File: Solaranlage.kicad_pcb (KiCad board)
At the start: 2 copper layers, 160 x 85 mm, 77 parts, among them J1 Screw_Terminal_01x02, J2 Screw_Terminal_01x02, J3 AVR-JTAG-10, J4 USB_B, J5 USB_B, J6 Screw_Terminal_01x02, Q1 2N3904, SW1 Rotary_Encoder_Switch_Panason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, SW2 SW_SPDT, U1 SC56-11E*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

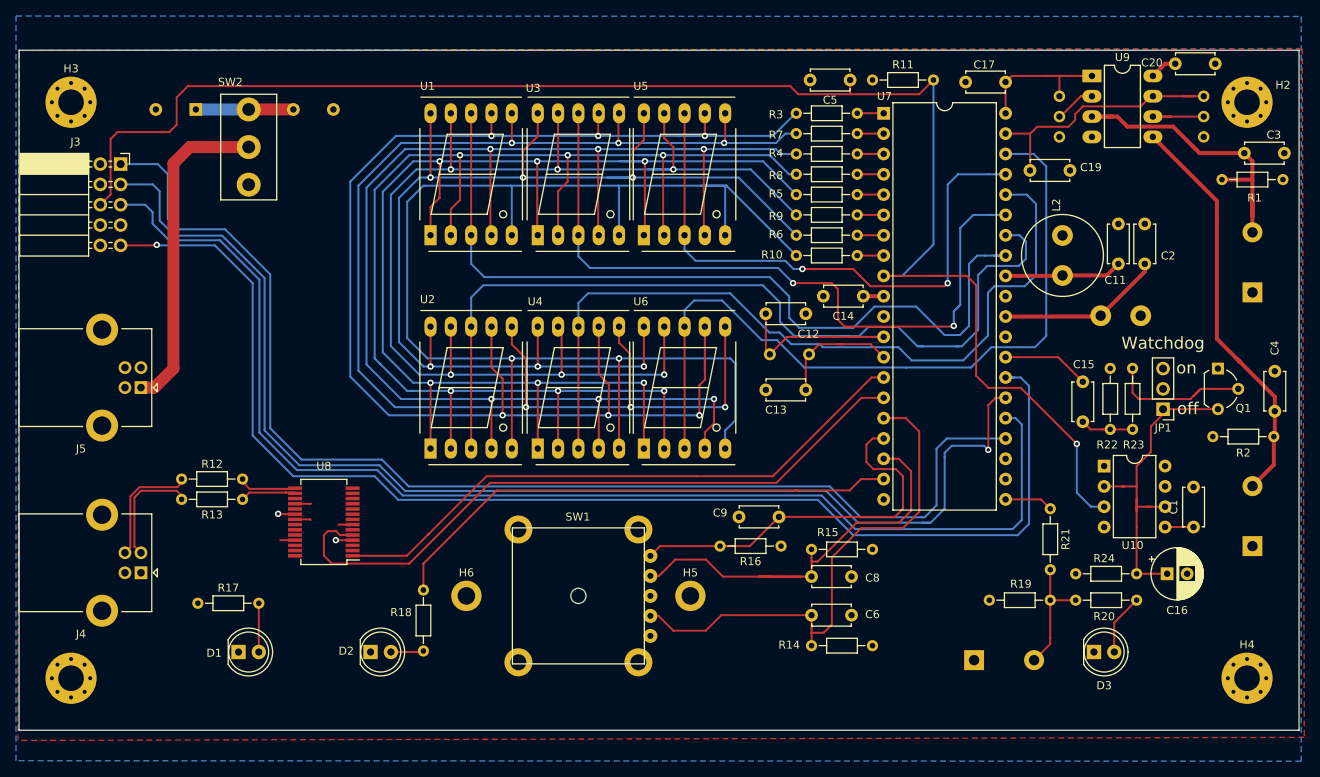
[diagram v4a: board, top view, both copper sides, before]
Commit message: added LEDs to indicate what the displays show at the moment; added some 3D models; added 10k serial resistors to opamp-outs for TP
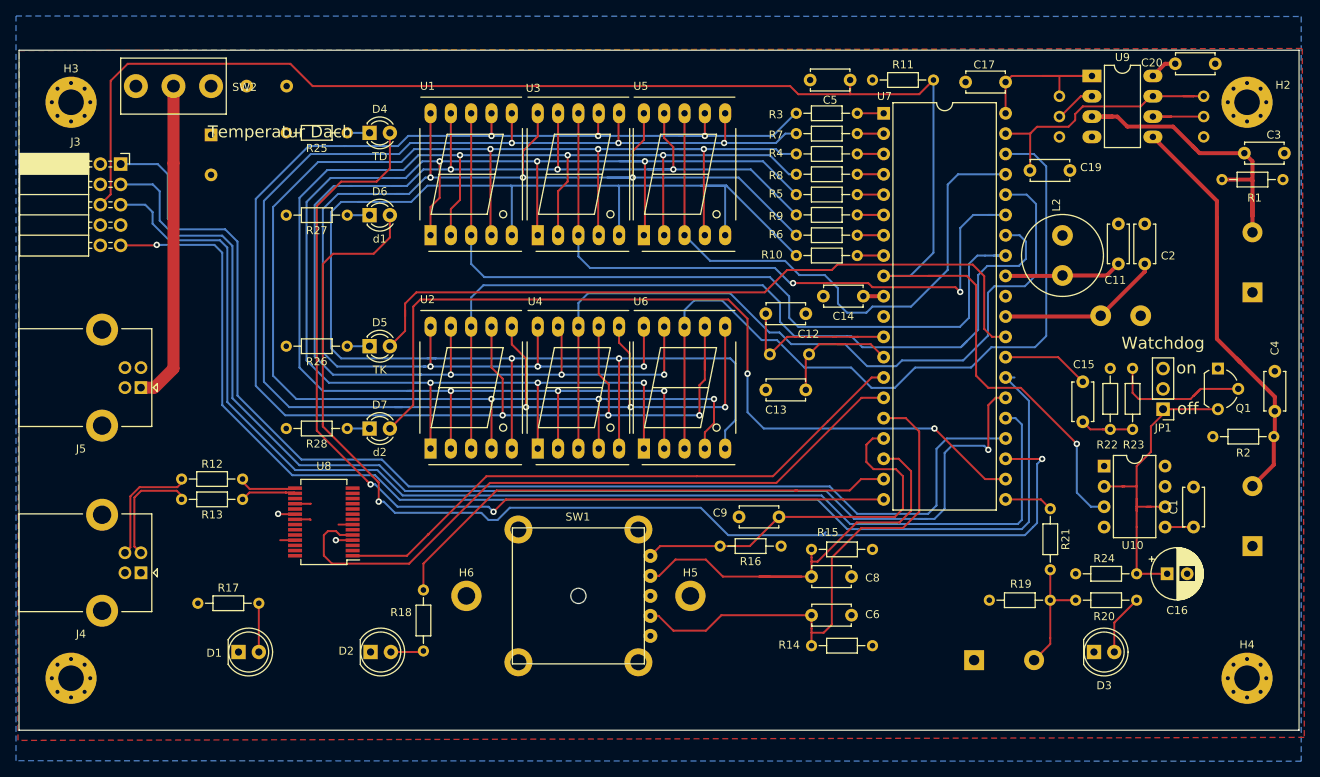
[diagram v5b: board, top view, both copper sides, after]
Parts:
- added D4: TD, LED_THT:LED_D3.0mm, F.Cu at (112.9, 65.5)
- added D5: TK, LED_THT:LED_D3.0mm, F.Cu at (112.9, 92.2)
- added D6: d1, LED_THT:LED_D3.0mm, F.Cu at (112.9, 75.8)
- added D7: d2, LED_THT:LED_D3.0mm, F.Cu at (112.9, 102.5)
- added R25: 330, Resistor_THT:R_Axial_DIN0204_L3.6mm_D1.6mm_P7.62mm_Horizontal, F.Cu at (110.1, 65.5)
- added R26: 330, Resistor_THT:R_Axial_DIN0204_L3.6mm_D1.6mm_P7.62mm_Horizontal, F.Cu at (110.1, 92.2)
- added R27: 330, Resistor_THT:R_Axial_DIN0204_L3.6mm_D1.6mm_P7.62mm_Horizontal, F.Cu at (110.1, 75.8)
- added R28: 330, Resistor_THT:R_Axial_DIN0204_L3.6mm_D1.6mm_P7.62mm_Horizontal, F.Cu at (110.1, 102.5)
- moved SW2 12.1 mm to (88.4, 59.7), turned to 180 degrees
- moved C7 6.53 mm to (97.5, 59.7)
- moved C18 3.70 mm to (93.1, 65.8), turned to 270 degrees
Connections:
- H1 pad 1: (no net) -> GND
- H2 pad 1: (no net) -> GND
- H3 pad 1: (no net) -> GND
- H4 pad 1: (no net) -> GND
- H5 pad 1: (no net) -> GND
- H6 pad 1: (no net) -> GND
- U7 pad 20: Net-(U7-Pad20) -> delta2
- U7 pad 22: Net-(U7-Pad22) -> temp_dach
- U7 pad 23: Net-(U7-Pad23) -> temp_keller
- U7 pad 29: Net-(U7-Pad29) -> delta1
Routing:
- net temp_keller: track 0.00 -> 145.1 mm, vias 0 -> 2
- net delta2: track 0.00 -> 119.3 mm, vias 0 -> 2
- net temp_dach: track 0.00 -> 107.0 mm, vias 0 -> 2
- net delta1: track 0.00 -> 93.0 mm
- net /C_2: track 178.0 -> 203.3 mm
- net /B_2: track 174.4 -> 198.7 mm
- net /A_2: track 176.9 -> 200.2 mm
- net /DP_2: track 168.2 -> 189.1 mm
- net /F_2: track 151.7 -> 172.3 mm
- net /G_2: track 147.6 -> 167.9 mm
- net /E_2: track 165.8 -> 185.8 mm
- net /D_2: track 179.9 -> 199.5 mm
- net +5V: track 22.6 -> 10.2 mm
- net /DZ: track 90.9 -> 82.3 mm
- net \RST: track 199.0 -> 204.2 mm
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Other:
- board text added: "Temperatur Dach"

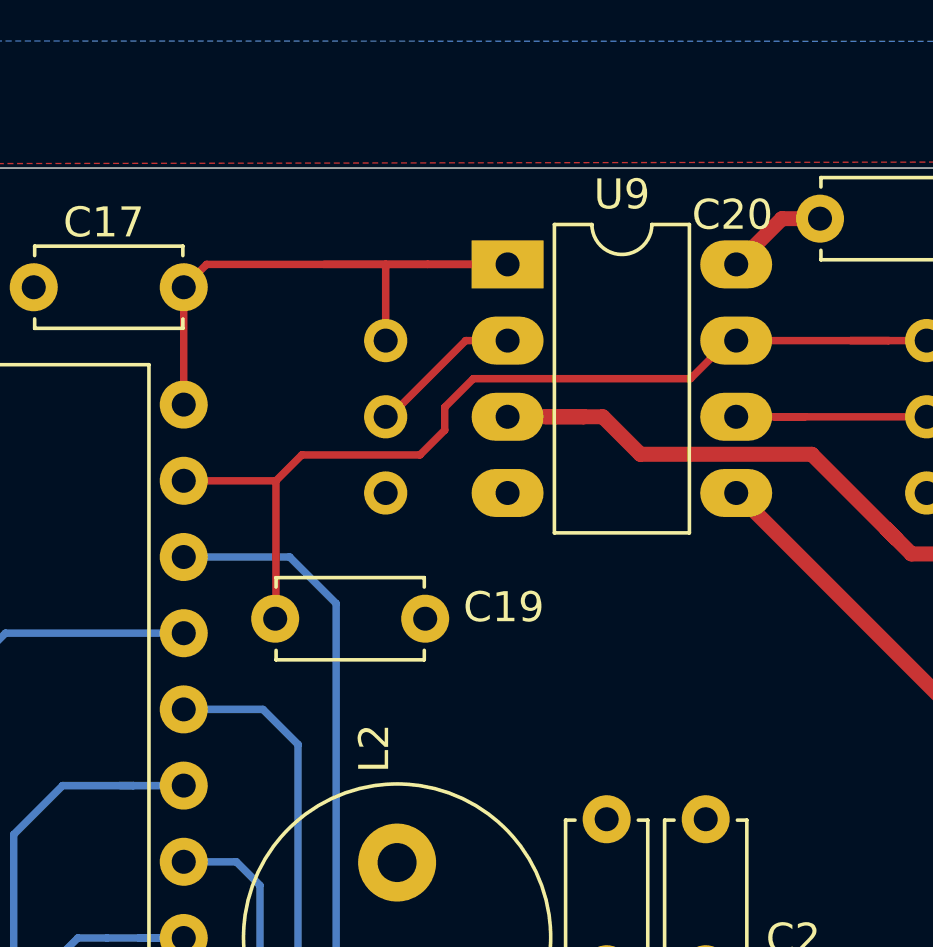
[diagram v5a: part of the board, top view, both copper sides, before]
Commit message: added resistors to layout
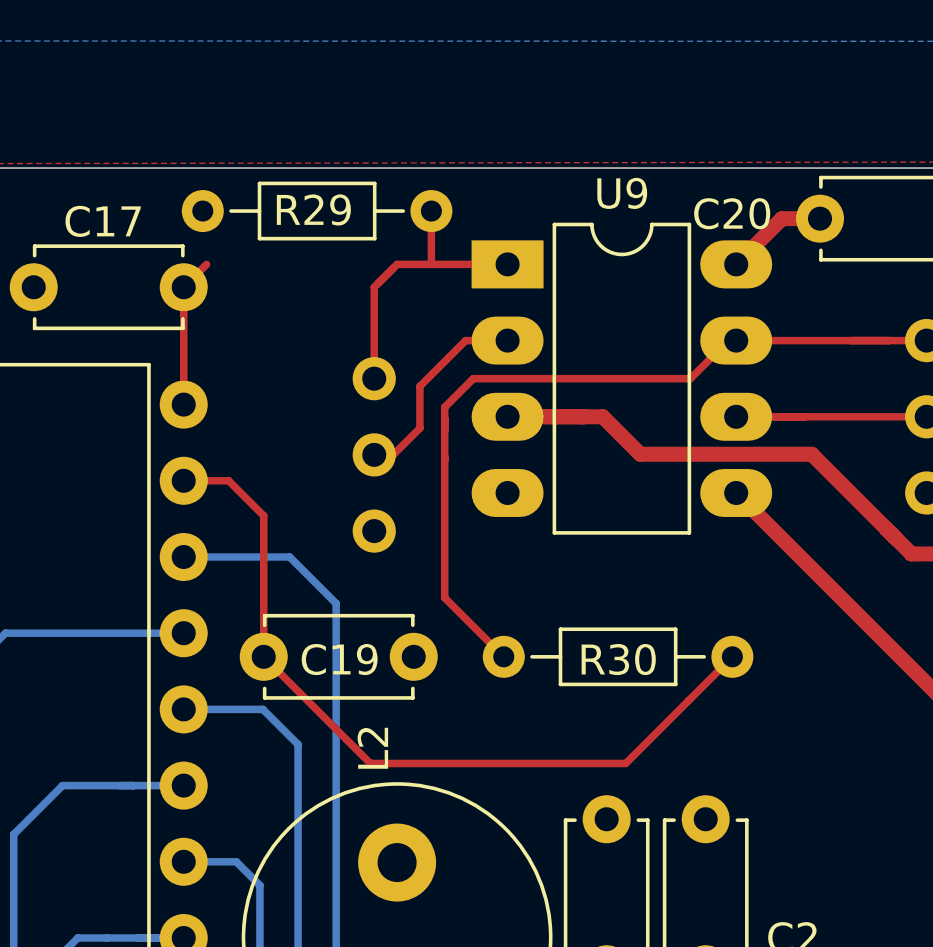
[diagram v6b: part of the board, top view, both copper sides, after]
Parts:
- added R29: 10k, Resistor_THT:R_Axial_DIN0204_L3.6mm_D1.6mm_P7.62mm_Horizontal, F.Cu at (193.0, 56.6)
- added R30: 10k, Resistor_THT:R_Axial_DIN0204_L3.6mm_D1.6mm_P7.62mm_Horizontal, F.Cu at (210.7, 71.5)
- C17, C19: value 10n -> 100n
- moved C19 1.33 mm to (195.1, 71.5)
- moved RV1 1.33 mm to (198.8, 62.2)
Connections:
- RV1 pad 1: /DACH_ADC -> Net-(R29-Pad2)
- RV2 pad 1: /KELLER_ADC -> Net-(R30-Pad2)
- U9 pad 1: /DACH_ADC -> Net-(R29-Pad2)
- U9 pad 7: /KELLER_ADC -> Net-(R30-Pad2)
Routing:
- net Net-(R30-Pad2): track 0.00 -> 27.9 mm
- net /DACH_ADC: track 23.7 -> 4.99 mm
- net Net-(R29-Pad2): track 0.00 -> 10.3 mm
- net /KELLER_ADC: track 33.1 -> 26.4 mm
- net Net-(RV1-Pad2): track 5.12 -> 6.84 mm

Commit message: optimization layout
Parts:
- moved RV2 1.27 mm to (217.2, 62.2)
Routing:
- net Net-(R30-Pad2): track 27.9 -> 33.5 mm
- net Net-(C3-Pad1): track 39.4 -> 38.5 mm
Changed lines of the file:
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@@
     (thickness 1.6)
     (drawings 14)
-    (tracks 866)
+    (tracks 868)
     (zones 0)
     (modules 87)
@@
   (setup
     (last_trace_width 0.25)
+    (user_trace_width 0)
     (user_trace_width 0.2)
     (user_trace_width 0.5)
+    (user_trace_width 0.5)
     (user_trace_width 1.5)
     (trace_clearance 0.2)
@@
   )
   (module Potentiometer_THT:Potentiometer_Bourns_3299W_Vertical (layer B.Cu)
-    (at 217.17 60.96 90)
+    (at 217.17 62.23 90)
     (descr "Potentiometer, vertical, Bourns 3299W, https://www.bourns.com/pdfs/3299.pdf")
     (tags "Potentiometer vertical Bourns 3299W")
@@
     (descr "Inductor, Radial series, Radial, pin pitch=5.00mm, , diameter=10mm, Fastron, 07P, http://www.fastrongroup.com/image-show/37/07M.pdf?type=Complete-DataSheet&productType=series")
     (tags "Inductor Radial series Radial pin pitch 5.00mm  diameter 10mm Fastron 07P")
-    (fp_text reference L2 (at -3.81 0.762 90) (layer F.SilkS)
+    (fp_text reference L2 (at -2.413 4.064 180) (layer F.SilkS)
       (effects (font (size 1 1) (thickness 0.15)))
     )
@@
   (segment (start 223.266 71.501) (end 223.266 70.612) (width 0.5) (layer F.Cu) (net 40))
   (segment (start 223.266 70.612) (end 223.266 69.088) (width 0.5) (layer F.Cu) (net 40))
-  (segment (start 216.662 68.072) (end 215.8365 67.2465) (width 0.5) (layer F.Cu) (net 40))
-  (segment (start 222.25 68.072) (end 216.662 68.072) (width 0.5) (layer F.Cu) (net 40))
-  (segment (start 216.154 67.564) (end 215.8365 67.2465) (width 0.5) (layer F.Cu) (net 40))
-  (segment (start 213.34001 64.75001) (end 207.62501 64.75001) (width 0.5) (layer F.Cu) (net 40))
-  (segment (start 207.62501 64.75001) (end 206.375 63.5) (width 0.5) (layer F.Cu) (net 40))
-  (segment (start 215.8365 67.2465) (end 213.34001 64.75001) (width 0.5) (layer F.Cu) (net 40))
   (segment (start 203.2 63.5) (end 205.74 63.5) (width 0.5) (layer F.Cu) (net 40))
   (segment (start 205.74 63.5) (end 204.47 63.5) (width 0.5) (layer F.Cu) (net 40))
   (segment (start 206.375 63.5) (end 205.74 63.5) (width 0.5) (layer F.Cu) (net 40))
+  (segment (start 212.57801 64.75001) (end 207.62501 64.75001) (width 0.5) (layer F.Cu) (net 40))
+  (segment (start 214.5665 66.7385) (end 212.57801 64.75001) (width 0.5) (layer F.Cu) (net 40))
+  (segment (start 214.5665 68.3895) (end 214.5665 66.7385) (width 0.5) (layer F.Cu) (net 40))
+  (segment (start 207.62501 64.75001) (end 206.375 63.5) (width 0.5) (layer F.Cu) (net 40))
+  (segment (start 217.551 71.374) (end 214.5665 68.3895) (width 0.5) (layer F.Cu) (net 40))
+  (segment (start 219.456 71.374) (end 217.551 71.374) (width 0.5) (layer F.Cu) (net 40))
   (segment (start 225.933 107.023) (end 223.266 109.69) (width 0.5) (layer F.Cu) (net 41))
   (segment (start 225.933 103.505) (end 225.933 107.023) (width 0.5) (layer F.Cu) (net 41))
@@
   (segment (start 226.06 100.33) (end 226.06 98.525) (width 0.5) (layer F.Cu) (net 41))
   (segment (start 221.565 94.03) (end 221.2475 93.7125) (width 0.5) (layer F.Cu) (net 41))
-  (segment (start 218.821 91.286) (end 221.7555 94.2205) (width 0.5) (layer F.Cu) (net 41))
   (segment (start 221.7555 94.2205) (end 221.565 94.03) (width 0.5) (layer F.Cu) (net 41))
   (segment (start 226.06 98.525) (end 221.7555 94.2205) (width 0.5) (layer F.Cu) (net 41))
-  (segment (start 218.821 74.041) (end 210.82 66.04) (width 0.5) (layer F.Cu) (net 41))
-  (segment (start 218.821 76.2) (end 218.821 74.041) (width 0.5) (layer F.Cu) (net 41))
-  (segment (start 218.821 76.2) (end 218.821 91.286) (width 0.5) (layer F.Cu) (net 41))
+  (segment (start 218.821 91.286) (end 221.7555 94.2205) (width 0.5) (layer F.Cu) (net 41))
+  (segment (start 218.821 75.819) (end 218.821 91.286) (width 0.5) (layer F.Cu) (net 41))
+  (segment (start 212.598 69.596) (end 218.821 75.819) (width 0.5) (layer F.Cu) (net 41))
+  (segment (start 212.598 67.818) (end 212.598 69.596) (width 0.5) (layer F.Cu) (net 41))
+  (segment (start 210.82 66.04) (end 212.598 67.818) (width 0.5) (layer F.Cu) (net 41))
   (segment (start 205.994 126.746) (end 208.788 123.952) (width 0.25) (layer F.Cu) (net 42))
   (segment (start 205.994 130.429) (end 205.994 126.746) (width 0.25) (layer F.Cu) (net 42))
@@
   (segment (start 193.167 58.42) (end 192.405 59.182) (width 0.25) (layer F.Cu) (net 43))
   (segment (start 214.63 60.96) (end 215.9 60.96) (width 0.25) (layer F.Cu) (net 92))
-  (segment (start 215.9 60.96) (end 217.17 60.96) (width 0.25) (layer F.Cu) (net 92))
   (segment (start 195.072 66.802) (end 193.9036 65.6336) (width 0.25) (layer F.Cu) (net 44))
   (segment (start 195.072 71.501) (end 195.072 66.802) (width 0.25) (layer F.Cu) (net 44))
@@
   (segment (start 199.39 64.77) (end 200.279 63.881) (width 0.25) (layer F.Cu) (net 80))
   (segment (start 198.755 64.77) (end 199.39 64.77) (width 0.25) (layer F.Cu) (net 80))
-  (segment (start 213.106 63.5) (end 210.82 63.5) (width 0.25) (layer F.Cu) (net 81))
-  (segment (start 212.09 63.5) (end 213.106 63.5) (width 0.25) (layer F.Cu) (net 81))
-  (segment (start 213.106 63.5) (end 217.17 63.5) (width 0.25) (layer F.Cu) (net 81))
+  (segment (start 217.17 64.77) (end 215.392 64.77) (width 0.25) (layer F.Cu) (net 81))
+  (segment (start 215.392 64.77) (end 214.122 63.5) (width 0.25) (layer F.Cu) (net 81))
+  (segment (start 214.122 63.5) (end 210.82 63.5) (width 0.25) (layer F.Cu) (net 81))
   (segment (start 196.8246 111.3536) (end 197.993 112.522) (width 0.25) (layer F.Cu) (net 82))
   (segment (start 192.405 111.3536) (end 196.8246 111.3536) (width 0.25) (layer F.Cu) (net 82))
@@
   (segment (start 201.1045 64.8335) (end 201.1045 69.5325) (width 0.25) (layer F.Cu) (net 92))
   (segment (start 201.1045 64.8335) (end 201.1045 64.9605) (width 0.25) (layer F.Cu) (net 92))
+  (segment (start 215.9 60.96) (end 217.17 62.23) (width 0.25) (layer F.Cu) (net 92))
+  (segment (start 210.82 60.96) (end 215.9 60.96) (width 0.25) (layer F.Cu) (net 92))
   (zone (net 2) (net_name +5V) (layer B.Cu) (hatch edge 0.508)
     (connect_pads (clearance 0.508))
